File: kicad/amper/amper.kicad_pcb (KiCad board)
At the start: 2 copper layers, 100 x 100 mm, 53 parts, among them J1 Conn_02x05_Odd_Even, J2 Conn_02x05_Odd_Even, J3 Conn_02x05_Odd_Even, J4 USB_C_Receptacle_USB2.0, J5 Conn_01x03, J6 Conn_01x04, J7 Conn_01x05, Q1 FDS9435A, Q2 FDS9435A, SW1 SW_Push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

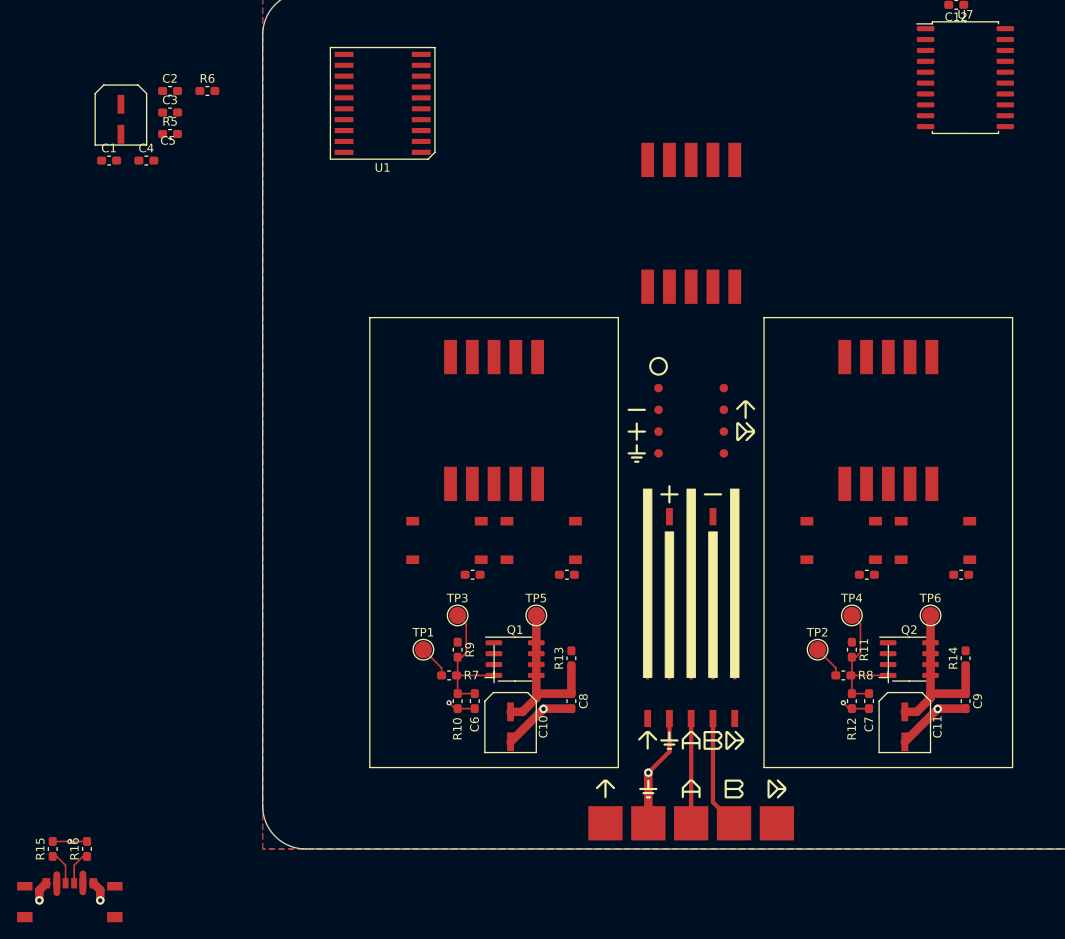
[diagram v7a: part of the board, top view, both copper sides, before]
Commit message: Added USB socket and boxes with A, B and output symbols. Local routing started
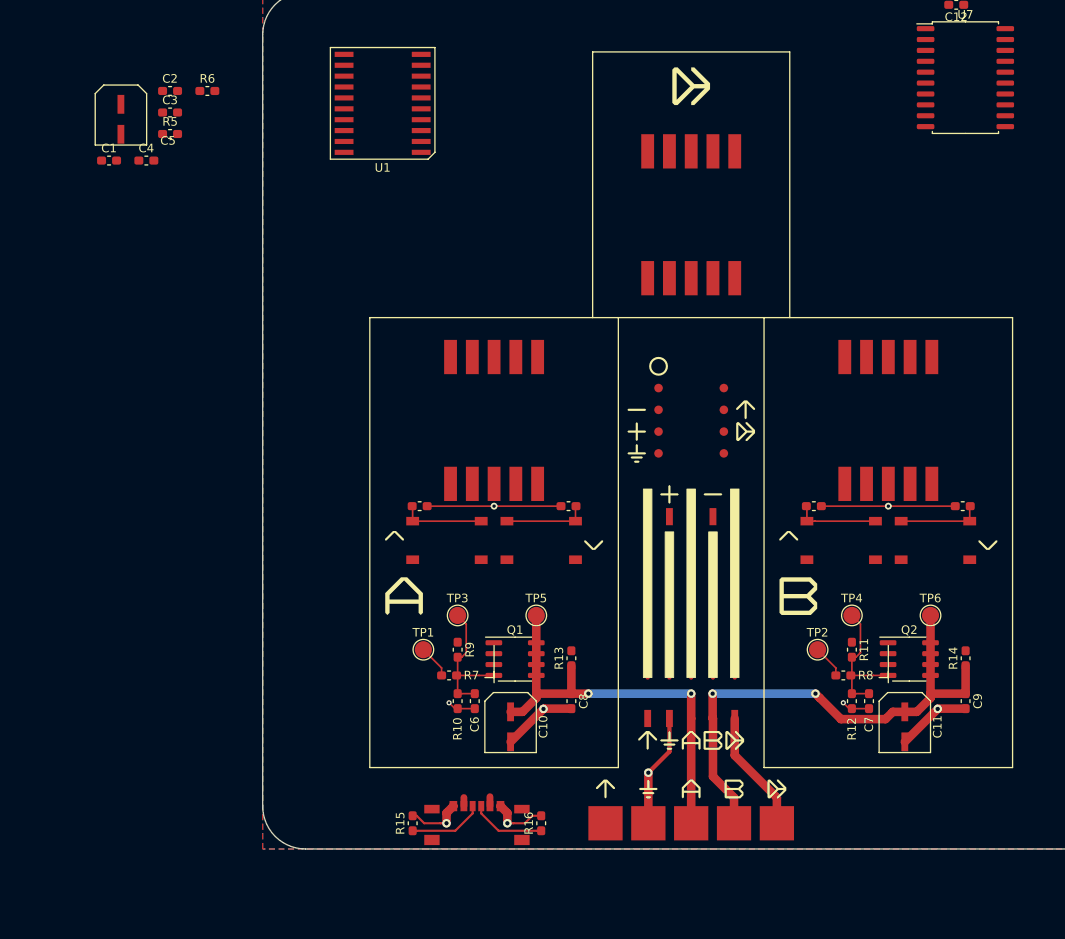
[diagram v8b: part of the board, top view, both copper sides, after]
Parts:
- added svg2mod: G***, amper:LargeOutput, F.Cu at (0.00, -39.0)
- added svg2mod: G***, amper:LargeB, F.Cu at (12.5, 20.5)
- added svg2mod: G***, amper:LargeA, F.Cu at (-33.5, 20.5)
- SW1, SW3: footprint amper:K2-1157SP-I4SW-01 -> amper:UpSwitch
- SW2, SW4: footprint amper:K2-1157SP-I4SW-01 -> amper:DnSwitch
- moved R16 53.1 mm to (-17.5, 47.0)
- moved J4 48.3 mm to (-25.0, 45.0)
- moved R15 42.1 mm to (-32.5, 47.0)
- moved R1 10.1 mm to (-31.7, 10.0), turned to 180 degrees
- moved R3 10.1 mm to (14.3, 10.0), turned to 180 degrees
- moved R2 8.00 mm to (-14.3, 10.0)
- moved R4 8.00 mm to (31.7, 10.0)
- moved SW1 1.19 mm to (-29.7, 14.0)
- moved SW2 1.19 mm to (-16.3, 14.0)
- moved SW3 1.19 mm to (16.3, 14.0)
- moved SW4 1.19 mm to (29.7, 14.0)
- moved U2 1.00 mm to (0.00, -24.0)
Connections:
- R1 pad 1: +5V -> GND
- R1 pad 2: Net-(R1-Pad2) -> /SourceAUp
- R2 pad 1: +5V -> GND
- R2 pad 2: Net-(R2-Pad2) -> /SourceADn
- R3 pad 1: +5V -> GND
- R3 pad 2: Net-(R3-Pad2) -> /SourceBUp
- R4 pad 1: +5V -> GND
- R4 pad 2: Net-(R4-Pad2) -> /SourceBDn
- SW1 pad 1: GND -> /SourceAUp
- SW1 pad 2: Net-(R1-Pad2) -> +5V
- SW2 pad 1: GND -> /SourceADn
- SW2 pad 2: Net-(R2-Pad2) -> +5V
- SW3 pad 1: GND -> /SourceBUp
- SW3 pad 2: Net-(R3-Pad2) -> +5V
- SW4 pad 1: GND -> /SourceBDn
- SW4 pad 2: Net-(R4-Pad2) -> +5V
- U7 pad 12: GND -> /SourceAUp
- U7 pad 13: GND -> /SourceADn
- U7 pad 14: GND -> /SourceBUp
- U7 pad 15: GND -> /SourceBDn
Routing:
- net GND: track 45.8 -> 81.6 mm, vias 8 -> 9
- net /SourceBOut: track 33.6 -> 60.5 mm, vias 0 -> 2
- net /SourceAOut: track 32.6 -> 49.5 mm, vias 0 -> 2
- net /ResultAdc: track 0.00 -> 14.3 mm
- net /SourceBUp: track 0.00 -> 9.77 mm
- net /SourceBDn: track 0.00 -> 9.77 mm
- net /SourceAUp: track 0.00 -> 9.77 mm
- net /SourceADn: track 0.00 -> 9.77 mm
- net Net-(J4-PadB5): track 4.02 -> 8.69 mm
- net Net-(J4-PadA5): track 4.02 -> 8.69 mm
- net +5V: track 4.20 -> 2.10 mm
